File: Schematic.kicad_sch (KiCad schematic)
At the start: 91 parts, among them J1 Screw_Terminal_01x04, J20 T44007, J21 T44007, Q1 HY1707, Q20 BC817, Q21 SUD50P06-15, U1 UC3845, U20 TCMT1108, U21 TL431M

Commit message: Sch update ongoing
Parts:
- removed D23: BZT52B5V1, Diode_SMD:D_SOD-123, symbol Device:D_Zener
- added C30: 220p, Capacitor_THT:C_Rect_L16.5mm_W5.0mm_P15.00mm_MKT, symbol Device:C
- added R31: 2k2, Resistor_SMD:R_0603_1608Metric_Pad0.98x0.95mm_HandSolder, symbol Device:R
- added R32, R33: 0, Resistor_SMD:R_0603_1608Metric_Pad0.98x0.95mm_HandSolder, symbol Device:R
- added R34: 470, Resistor_THT:R_Axial_DIN0918_L18.0mm_D9.0mm_P7.62mm_Vertical, symbol Device:R
- added R35: 20m, Resistor_SMD:R_Shunt_Vishay_WSR2_WSR3, symbol Device:R
- C2: now not fitted
- C20: value 6.8p -> 100n
- C21: value 22p -> 100p
- C24, C27: footprint Capacitor_SMD:C_0805_2012Metric_Pad1.18x1.45mm_HandSolder -> Capacitor_SMD:C_1206_3216Metric_Pad1.33x1.80mm_HandSolder
- C3: value 3n3 -> 1n
- C4: value 1.5n -> 1n
- R20: value 15M -> 100k
- R26: value 1k -> 4.7k
- R28: now fitted
- R29: value 0 -> 1k; now not fitted
- R3: value 5k -> 10k
- R5: value 5k1 -> 15k
- R8: footprint Resistor_SMD:R_0603_1608Metric_Pad0.98x0.95mm_HandSolder -> Resistor_SMD:R_1206_3216Metric_Pad1.30x1.75mm_HandSolder
- R9: footprint Resistor_THT:R_Axial_DIN0309_L9.0mm_D3.2mm_P15.24mm_Horizontal -> Personal:Shunt_alixp_module
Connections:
- net Comp: now also R33.2
- net OpCol: now also R33.1
- net OpEm: now also R32.1; no longer C25.1
- net PWM: now also R31.2
- net Ramp: now also R31.1
- net Sec_ref_sns: now also C21.1
- net Src: now also R35.1
- net U0: now also R35.2
- net U500_sec: now also C30.2
- net U500_tr_sec: now also R34.2
- net Sec_comp_mid renamed Sec_cp_m
- net Sec_cp_m: no longer C21.1
- new net: C25.1, R32.2
- new net U500_sn_sec: C30.1, R34.1
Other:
- note added: "Alternative supply"
- note added: "Error amplifier bypass"
- note removed: "Feed forward"
- moved on the sheet: C20, C21, C22, C23, C24, C25, C26, C27, C28, C29, C3, C4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

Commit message: Further sch changes
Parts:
- C6: footprint Capacitor_SMD:C_0805_2012Metric_Pad1.18x1.45mm_HandSolder -> Capacitor_SMD:C_1206_3216Metric_Pad1.33x1.80mm_HandSolder
- R23: value 1k -> 470
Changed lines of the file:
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@@
 			)
 		)
-		(property "Footprint" "Capacitor_SMD:C_0805_2012Metric_Pad1.18x1.45mm_HandSolder"
+		(property "Footprint" "Capacitor_SMD:C_1206_3216Metric_Pad1.33x1.80mm_HandSolder"
 			(at 160.9852 104.14 0)
 			(effects
@@
 			)
 		)
-		(property "Value" "1k"
+		(property "Value" "470"
 			(at 80.01 124.46 0)
 			(effects

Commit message: Schematic nearly complete
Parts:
- removed C23: 100u, Capacitor_THT:CP_Radial_D6.3mm_P2.50mm, symbol Device:C_Polarized
- removed D21: 1N4148W, Diode_SMD:D_SOD-123, symbol Diode:1N4148W
- removed P33: ~, symbol personal:Cosmetic_PWR
- removed R27: 15k, Resistor_SMD:R_0603_1608Metric_Pad0.98x0.95mm_HandSolder, symbol Device:R
- removed TP21, TP22, TP29: TestPoint_Alt, TestPoint:TestPoint_Loop_D3.50mm_Drill0.9mm_Beaded, symbol Connector:TestPoint_Alt
- added C31: 2.7n, Capacitor_SMD:C_1206_3216Metric_Pad1.33x1.80mm_HandSolder, symbol Device:C
- added C32: 1u, Capacitor_SMD:C_0805_2012Metric_Pad1.18x1.45mm_HandSolder, symbol Device:C
- added P27: ~, symbol personal:Cosmetic_PWR_SRC
- added Q22: BC857, Package_TO_SOT_SMD:SOT-23, symbol Transistor_BJT:BC857
- added R36, R37, R38: 33, Resistor_SMD:R_1206_3216Metric_Pad1.30x1.75mm_HandSolder, symbol Device:R
- added R39, R40, R41: 470, Resistor_SMD:R_1206_3216Metric_Pad1.30x1.75mm_HandSolder, symbol Device:R
- added TP35, TP36: ~, Personal:Testpoint_osc_no_lead, symbol personal:OscTestpoint
- C30: footprint Capacitor_THT:C_Rect_L16.5mm_W5.0mm_P15.00mm_MKT -> Capacitor_SMD:C_1206_3216Metric_Pad1.33x1.80mm_HandSolder
- R34: value 470 -> 0; footprint Resistor_THT:R_Axial_DIN0918_L18.0mm_D9.0mm_P7.62mm_Vertical -> Resistor_SMD:R_0603_1608Metric_Pad0.98x0.95mm_HandSolder
- R35: value 20m -> 100k; footprint Resistor_SMD:R_Shunt_Vishay_WSR2_WSR3 -> Resistor_SMD:R_0603_1608Metric_Pad0.98x0.95mm_HandSolder; now fitted
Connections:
- net Comp: now also Q22.2 (E)
- net Isns: now also TP35.1 (Sig)
- net SW: now also R36.1, R37.1, R38.1
- net Sec_ref_sns: now also R34.2; no longer R11.1
- net Src: now also C31.1, TP36.1 (Sig); no longer R35.1
- net U0: now also C32.2, Q22.3 (C), TP35.2 (Ref), TP36.2 (Ref); no longer R35.2
- net U500_sn_sec: now also R39.1, R40.1, R41.1; no longer R34.1
- net U500_tr_sec: now also R39.2, R40.2, R41.2; no longer R34.2
- net U5_ref: now also R35.1, P27.1
- new net: C31.2, R36.2, R37.2, R38.2
- new net: C32.1, Q22.1 (B), R35.2
- new net Sec_div_h2: R11.1, R34.1
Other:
- moved on the sheet: C24, C27, C28, C29, C30, C8, J1, Mod20, R10, R11, R12, R30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

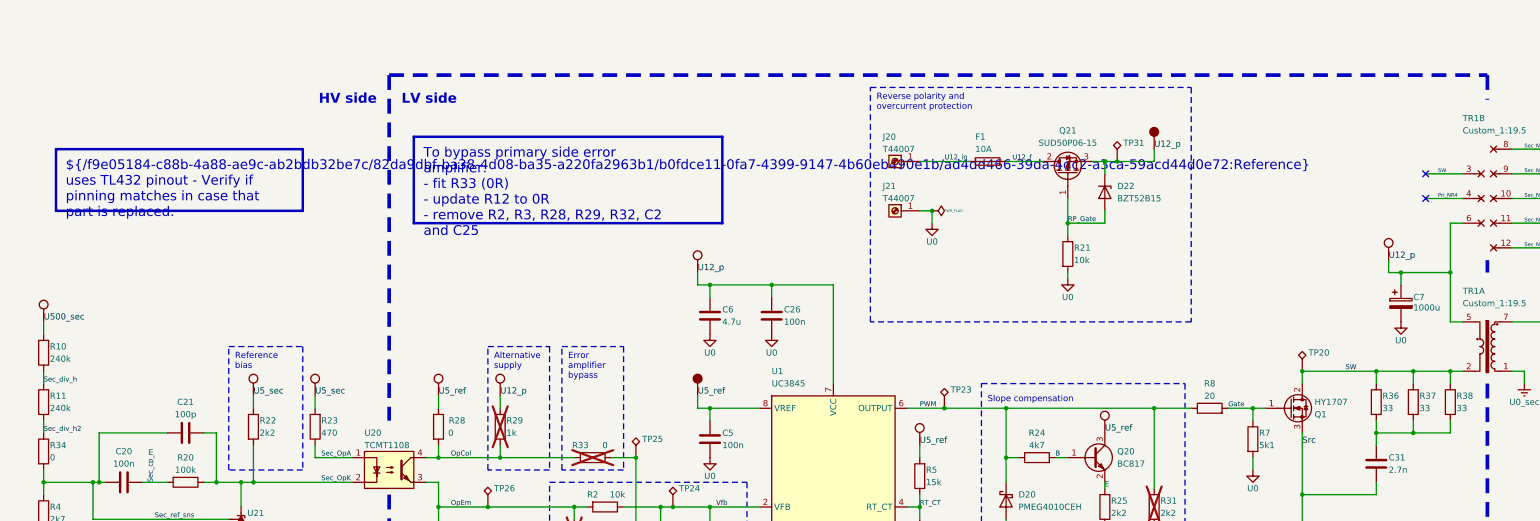
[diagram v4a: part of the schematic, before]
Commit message: added perfboard
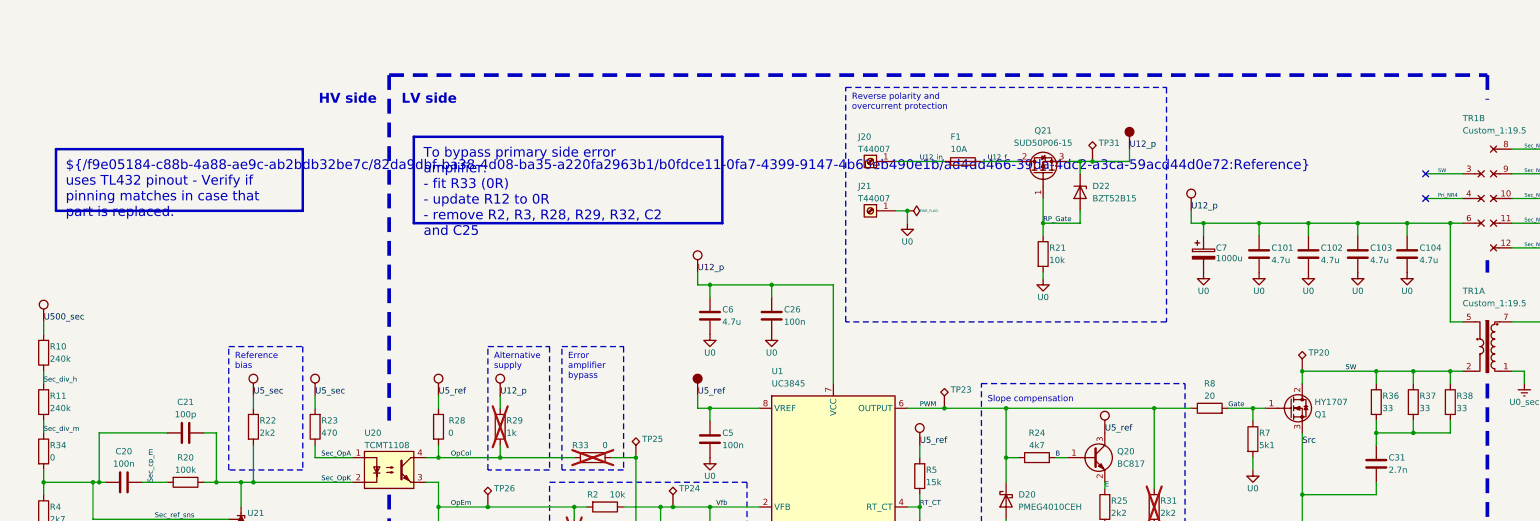
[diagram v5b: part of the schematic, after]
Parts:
- added C101, C102, C103, C104: 4.7u, Capacitor_SMD:C_1206_3216Metric_Pad1.33x1.80mm_HandSolder, symbol Device:C
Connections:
- net U0: now also C101.2, C102.2, C103.2, C104.2
- net U12_p: now also C101.1, C102.1, C103.1, C104.1
- net Sec_div_h2 renamed Sec_div_m
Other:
- moved on the sheet: C7, D22, F1, J20, J21, Q21, R21, TP31

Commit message: layout update started
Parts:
- added P101: ~, symbol personal:Cosmetic_IN
- added P102: Out_signal, symbol personal:Cosmetic_OUT
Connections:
- net SW: now also P101.1, P102.1
- no-connect marks 9 -> 8
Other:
- moved on the sheet: TP35, TP36

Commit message: Updating mfg drw
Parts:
- added D8: S15M, Diode_SMD:D_SMC, symbol Device:D
- added TP10, TP9: TestPoint_Alt, TestPoint:TestPoint_Loop_D3.50mm_Drill0.9mm_Beaded, symbol Connector:TestPoint_Alt
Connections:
- net Sec_OpK: now also TP10.1
- net Sec_ref_sns: now also TP9.1
- net U0_sec: now also D8.2 (A)
- net U500_sec: now also D8.1 (K)
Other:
- moved on the sheet: C21, C8, J1, R10, R11, TP28, TP32, TP33

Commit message: Updated rev history
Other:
- note added: "${/f9e05184-c88b-4a88-ae9c-ab2bdb32be7c/82da9dbf-ba38-4d08-ba35-a220fa2963b1/b0fdce11-0fa7-4399-9147-4b60eb490e1b/ad4dd466-39da-4dc2-a3ca-59acd44d0e72:reference} bias"
- note added: "Artificial ramp"
- note added: "Opto supply selection"
- note removed: "Alternative supply"
- note removed: "Reference bias"
- note removed: "Slope compensation"
- moved on the sheet: C101, C102, C103, C104, C2, C24, C27, C28, C29, C30, C31, C7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
